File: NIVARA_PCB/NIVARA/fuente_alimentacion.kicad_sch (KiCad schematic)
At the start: 11 parts, among them U1 AP63203WU

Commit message: se agregaron partnumbers
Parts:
- U1: PART NUMBERT (none) -> AP63203WU-7
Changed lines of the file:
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@@
 			)
 		)
-		(property "PART NUMBERT" ""
+		(property "PART NUMBERT" "AP63203WU-7"
 			(at 83.82 68.58 0)
 			(effects

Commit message: RS_485 ADD MODULE
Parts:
- C4, C5: PART NUMBERT (none) -> MSASL21GBC6226MTNA01
- R1, R2: PART NUMBERT (none) -> RC0603FR-0722KL
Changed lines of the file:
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@@
 			)
 		)
-		(property "PART NUMBERT" ""
+		(property "PART NUMBERT" "RC0603FR-0722KL"
 			(at 125.73 68.58 0)
 			(effects
@@
 					(size 1.27 1.27)
 				)
+				(hide yes)
 			)
 		)
@@
 			)
 		)
-		(property "PART NUMBERT" ""
+		(property "PART NUMBERT" "MSASL21GBC6226MTNA01"
 			(at 151.13 68.58 0)
 			(effects
@@
 					(size 1.27 1.27)
 				)
+				(hide yes)
 			)
 		)
@@
 			)
 		)
-		(property "PART NUMBERT" ""
+		(property "PART NUMBERT" "RC0603FR-0722KL"
 			(at 125.73 78.74 0)
 			(effects
@@
 					(size 1.27 1.27)
 				)
+				(hide yes)
 			)
 		)
@@
 					(size 1.27 1.27)
 				)
+				(hide yes)
 			)
 		)
@@
 			)
 		)
-		(property "PART NUMBERT" ""
+		(property "PART NUMBERT" "MSASL21GBC6226MTNA01"
 			(at 137.16 68.58 0)
 			(effects
@@
 					(size 1.27 1.27)
 				)
-			)
-		)
+				(hide yes)
+			)
+		)

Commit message: ACTUALIZACION
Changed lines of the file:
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@@
+	(wire
+		(pts
+			(xy 62.23 63.5) (xy 62.23 66.04)
+		)
+		(stroke
+			(width 0)
+			(type default)
+		)
+	)
 	(wire
 		(pts
@@
 			(width 0)
 			(type default)
+		)
+	)
+	(hierarchical_label "GND"
+		(shape input)
+		(at 62.23 76.2 180)
+		(effects
+			(font
+				(size 1.27 1.27)
+			)
+			(justify right)
+		)
+	)
+	(hierarchical_label "VCC"
+		(shape input)
+		(at 62.23 64.77 180)
+		(effects
+			(font
+				(size 1.27 1.27)
+			)
+			(justify right)
 		)
 	)
@@
 	(symbol
 		(lib_id "power:VCC")
-		(at 62.23 66.04 0)
+		(at 62.23 63.5 0)
 		(unit 1)
 		(exclude_from_sim no)
@@
 		(fields_autoplaced yes)
 		(property "Reference" "#PWR07"
-			(at 62.23 69.85 0)
+			(at 62.23 67.31 0)
 			(effects
 				(font
@@
 		)
 		(property "Value" "VCC"
-			(at 62.23 60.96 0)
+			(at 62.23 58.42 0)
 			(effects
 				(font
@@
 		)
 		(property "Footprint" ""
-			(at 62.23 66.04 0)
+			(at 62.23 63.5 0)
 			(effects
 				(font
@@
 		)
 		(property "Datasheet" ""
-			(at 62.23 66.04 0)
+			(at 62.23 63.5 0)
 			(effects
 				(font
@@
 		)
 		(property "Description" "Power symbol creates a global label with name \"VCC\""
-			(at 62.23 66.04 0)
-			(effects
-				(font
+			(at 62.23 63.5 0)
+			(effects
+				(font

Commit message: ACTUALIZACION
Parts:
- TP1: footprint TestPoint:TestPoint_THTPad_1.0x1.0mm_Drill0.5mm -> TestPoint:TestPoint_THTPad_D1.0mm_Drill0.5mm
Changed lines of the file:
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@@
-		)
-	)
-	(hierarchical_label "GND"
-		(shape input)
-		(at 62.23 76.2 180)
-		(effects
-			(font
-				(size 1.27 1.27)
-			)
-			(justify right)
-		)
-	)
-	(hierarchical_label "VCC"
-		(shape input)
-		(at 62.23 64.77 180)
-		(effects
-			(font
-				(size 1.27 1.27)
-			)
-			(justify right)
 		)
 	)
@@
 			)
 		)
-		(property "Footprint" "TestPoint:TestPoint_THTPad_1.0x1.0mm_Drill0.5mm"
+		(property "Footprint" "TestPoint:TestPoint_THTPad_D1.0mm_Drill0.5mm"
 			(at 132.08 55.88 0)
 			(effects

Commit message: SALIDAS DE VOLTAJE Y CORRIENTE
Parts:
- C3: value C_0603 -> 1uF; PART NUMBERT (none) -> CL10A105KB8NNNC
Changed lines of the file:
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@@
 			)
 		)
-		(property "Value" "C_0603"
+		(property "Value" "1uF"
 			(at 119.38 69.8499 0)
 			(effects
@@
 			)
 		)
-		(property "PART NUMBERT" ""
+		(property "PART NUMBERT" "CL10A105KB8NNNC"
 			(at 115.57 68.58 0)
 			(effects

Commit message: ACTUALIZACION
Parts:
- removed C1: 10uF, PCM_Capacitor_SMD_AKL:C_0603_1608Metric, symbol PCM_Capacitor_AKL:C_0603
- removed C3: 1uF, PCM_Capacitor_SMD_AKL:C_0603_1608Metric, symbol PCM_Capacitor_AKL:C_0603
- removed L1: L_Iron, Inductor_SMD:L_0201_0603Metric_Pad0.64x0.40mm_HandSolder, symbol Device:L_Iron
- removed R1, R2: 22K, PCM_Resistor_SMD_AKL:R_0603_1608Metric, symbol PCM_Resistor_AKL:R_0603
- added C1: 10uF, PCM_Capacitor_SMD_AKL:C_1206_3216Metric, symbol PCM_Capacitor_US_AKL:C_1206
- added L2: FNR5020S3R9NT, easyeda2kicad:IND-SMD_L5.0-W5.0_FNR50XXS, symbol easyeda2kicad:FNR5020S3R9NT
- C2: PART NUMBERT (none) -> CC0603KRX7R9BB104
- C4, C5: footprint PCM_Capacitor_SMD_AKL:C_0603_1608Metric -> PCM_Capacitor_SMD_AKL:C_0805_2012Metric; PART NUMBERT MSASL21GBC6226MTNA01 -> CL10A226MP8NUNE
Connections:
- net GND: now also C1.2
- net VCC: now also C1.1
- net at C4.1, C5.1, JP1.1 (A): now also U1.1 (FB), L2.2
- net at C2.2, U1.5 (SW): now also L2.1
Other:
- moved on the sheet: C4, C5

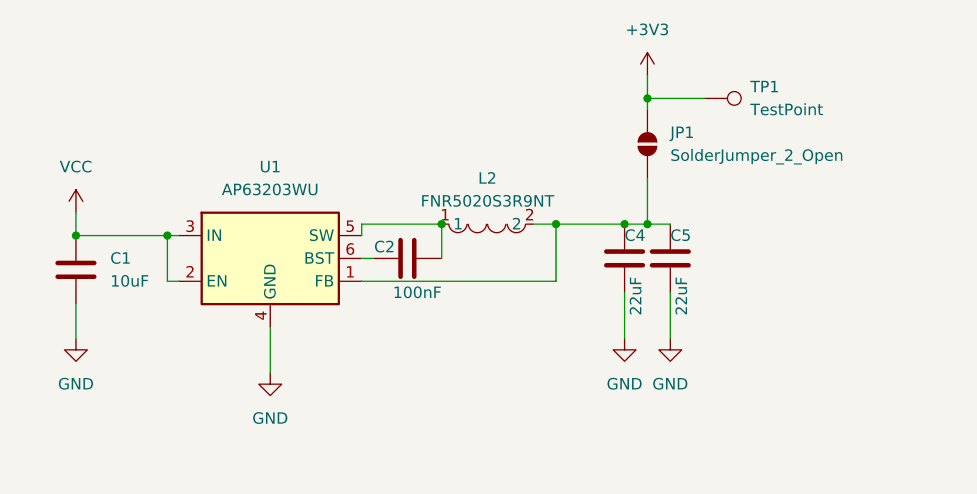
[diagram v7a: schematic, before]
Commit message: arreglo del desastre que tenia con las salidas PNP
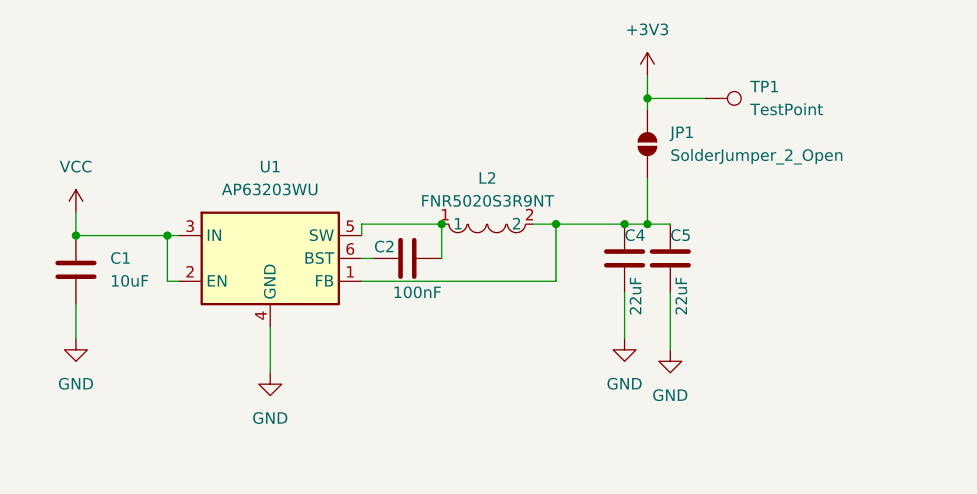
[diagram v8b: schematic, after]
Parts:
- C4, C5: footprint PCM_Capacitor_SMD_AKL:C_0805_2012Metric -> PCM_Capacitor_SMD_AKL:C_0603_1608Metric
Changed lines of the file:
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@@
 	(wire
 		(pts
-			(xy 128.27 72.39) (xy 128.27 77.47)
+			(xy 128.27 72.39) (xy 128.27 78.74)
 		)
 		(stroke
@@
 			)
 		)
-		(property "Footprint" "PCM_Capacitor_SMD_AKL:C_0805_2012Metric"
+		(property "Footprint" "PCM_Capacitor_SMD_AKL:C_0603_1608Metric"
 			(at 129.2352 72.39 0)
 			(effects
@@
 			)
 		)
-		(property "Footprint" "PCM_Capacitor_SMD_AKL:C_0805_2012Metric"
+		(property "Footprint" "PCM_Capacitor_SMD_AKL:C_0603_1608Metric"
 			(at 124.1552 72.39 0)
 			(effects
@@
 	(symbol
 		(lib_id "power:GND")
-		(at 128.27 77.47 0)
+		(at 128.27 78.74 0)
 		(unit 1)
 		(exclude_from_sim no)
@@
 		(fields_autoplaced yes)
 		(property "Reference" "#PWR01"
+			(at 128.27 85.09 0)
+			(effects
+				(font
+					(size 1.27 1.27)
+				)
+				(hide yes)
+			)
+		)
+		(property "Value" "GND"
 			(at 128.27 83.82 0)
 			(effects
@@
 					(size 1.27 1.27)
 				)
-				(hide yes)
-			)
-		)
-		(property "Value" "GND"
-			(at 128.27 82.55 0)
-			(effects
-				(font
-					(size 1.27 1.27)
-				)
 			)
 		)
 		(property "Footprint" ""
-			(at 128.27 77.47 0)
+			(at 128.27 78.74 0)
 			(effects
 				(font
@@
 		)
 		(property "Datasheet" ""
-			(at 128.27 77.47 0)
+			(at 128.27 78.74 0)
 			(effects
 				(font
@@
 		)
 		(property "Description" "Power symbol creates a global label with name \"GND\" , ground"
-			(at 128.27 77.47 0)
-			(effects
-				(font
+			(at 128.27 78.74 0)
+			(effects
+				(font
